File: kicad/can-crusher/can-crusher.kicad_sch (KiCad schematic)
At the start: 22 parts, among them J1 Stepper Right, J2 Control UART, J3 Ext power, J4 Stepper Left, J5 Barrel_Jack, J6 Expansion Port, Q1 IRF9540N, Q2 MMBF170, SW1 Reboot, SW2 User Interaction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

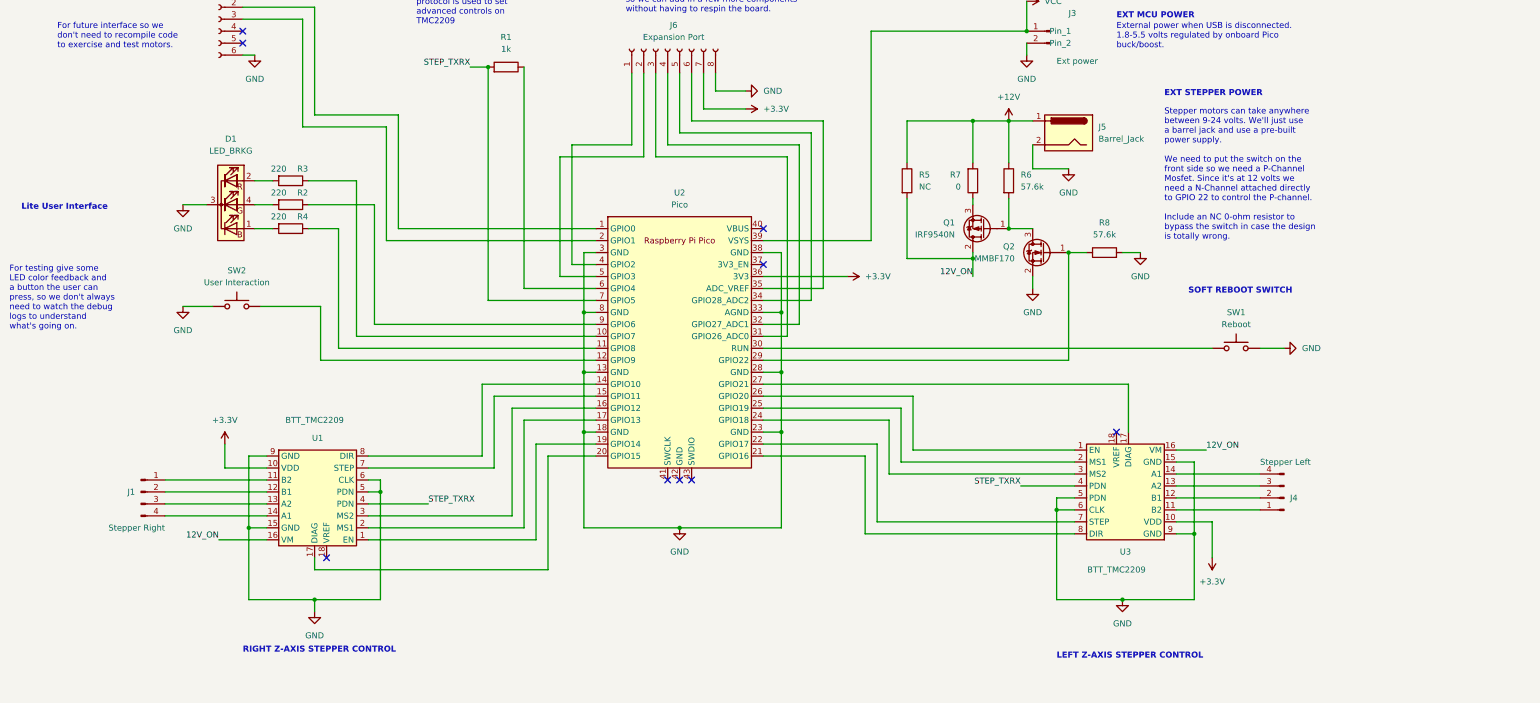
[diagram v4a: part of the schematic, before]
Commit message: Add fuse, power switch, and electrolytic caps
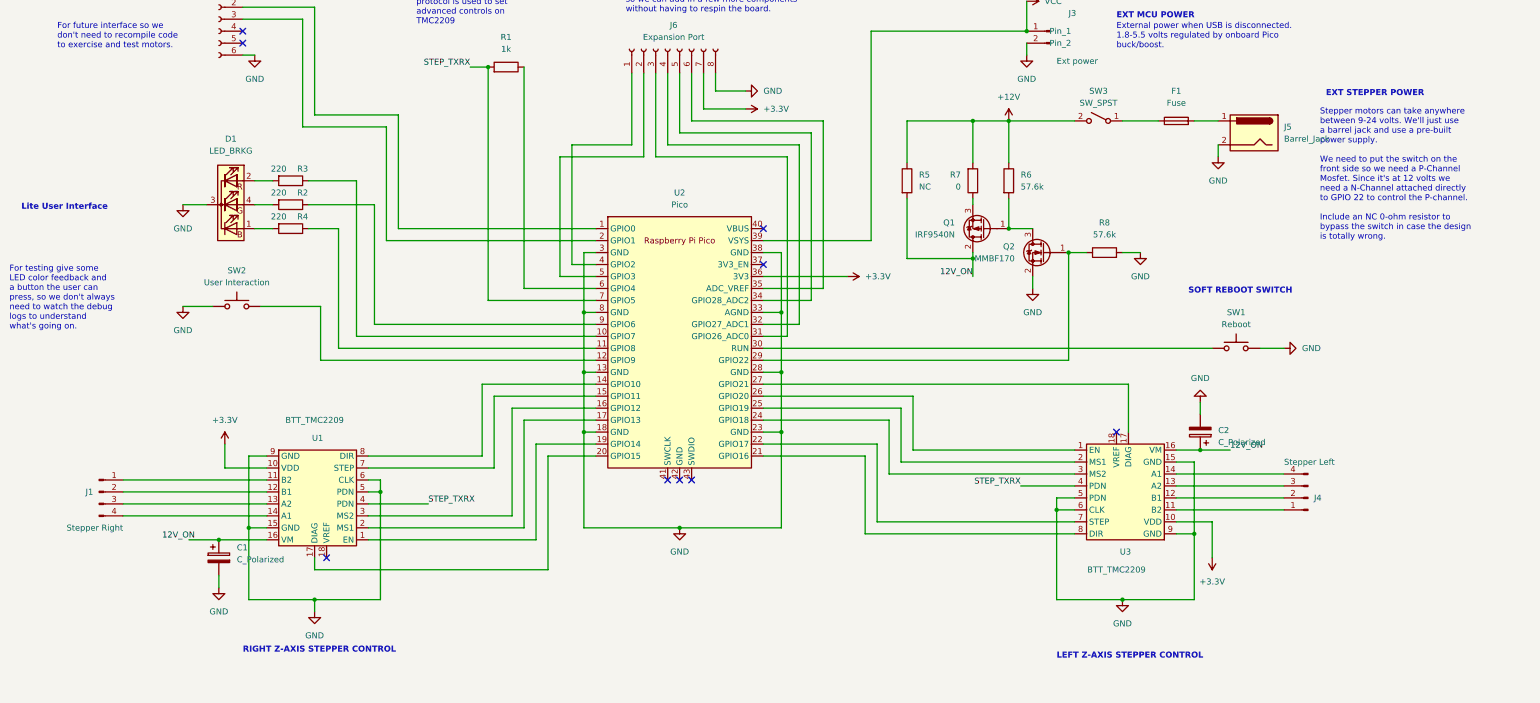
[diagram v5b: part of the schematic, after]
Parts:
- added C1, C2: C_Polarized, Capacitor_THT:CP_Radial_D6.3mm_P2.50mm, symbol Device:C_Polarized
- added F1: Fuse, Fuse:Fuse_Blade_Mini_directSolder, symbol Device:Fuse
- added SW3: SW_SPST, R1966:SW_R1966ABLKBLKGR, symbol Switch:SW_SPST
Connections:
- net +12V: now also SW3.2 (B); no longer J5.1
- net 12V_ON: now also C1.1, C2.1
- net GND: now also C1.2, C2.2
- new net: F1.1, SW3.1 (A)
- new net: F1.2, J5.1
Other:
- moved on the sheet: J1, J4, J5

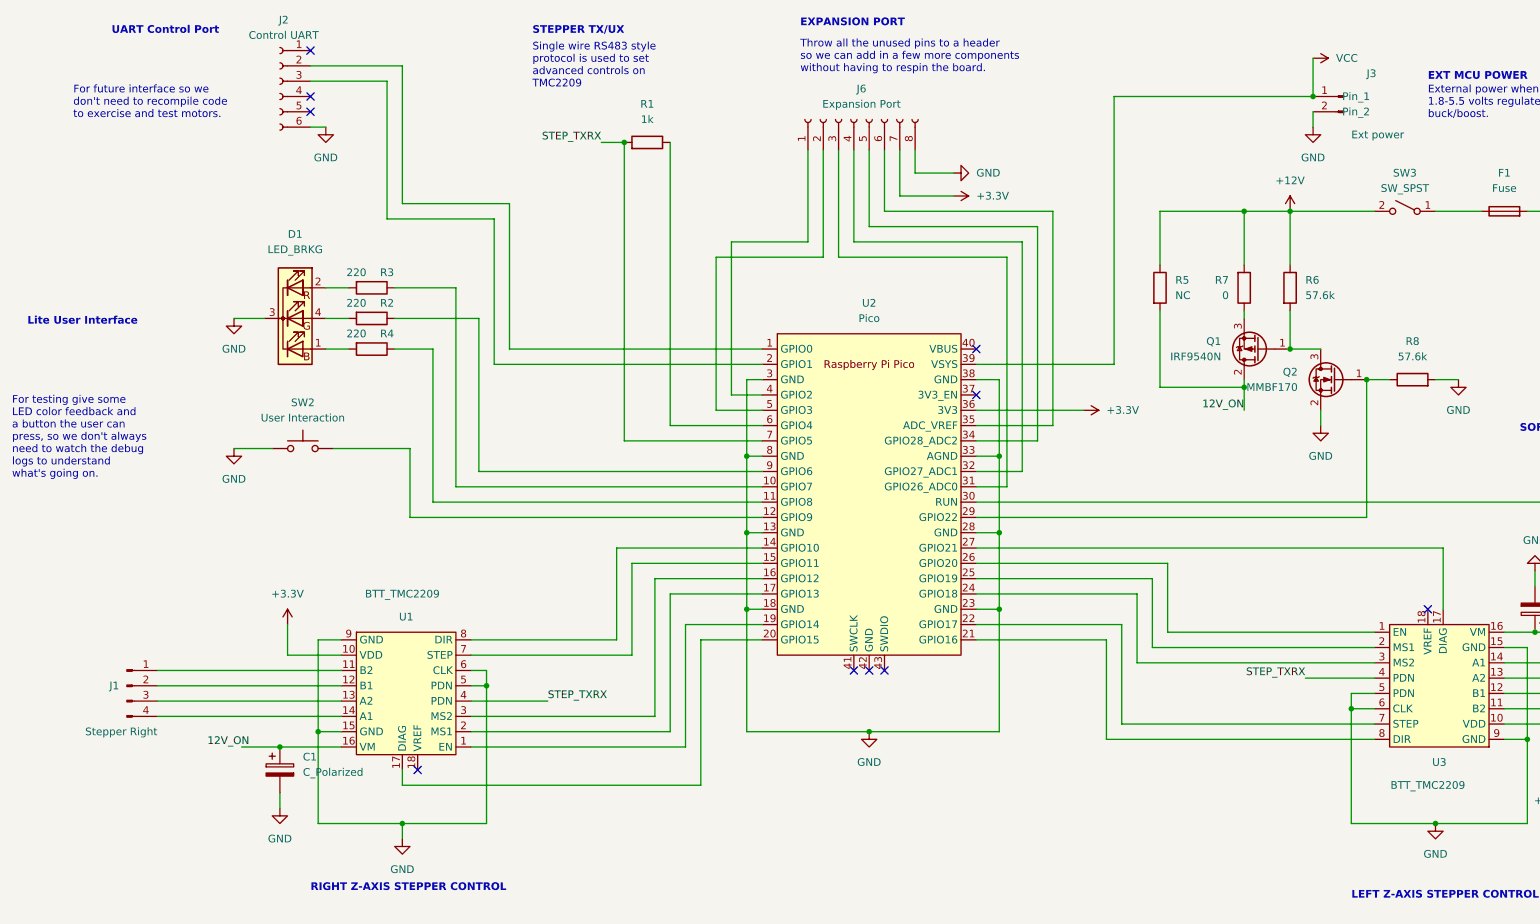
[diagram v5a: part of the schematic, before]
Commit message: Remove RGB led and button; add free pins to header; add ADC pins to the TMC2209 VREF pins for future use
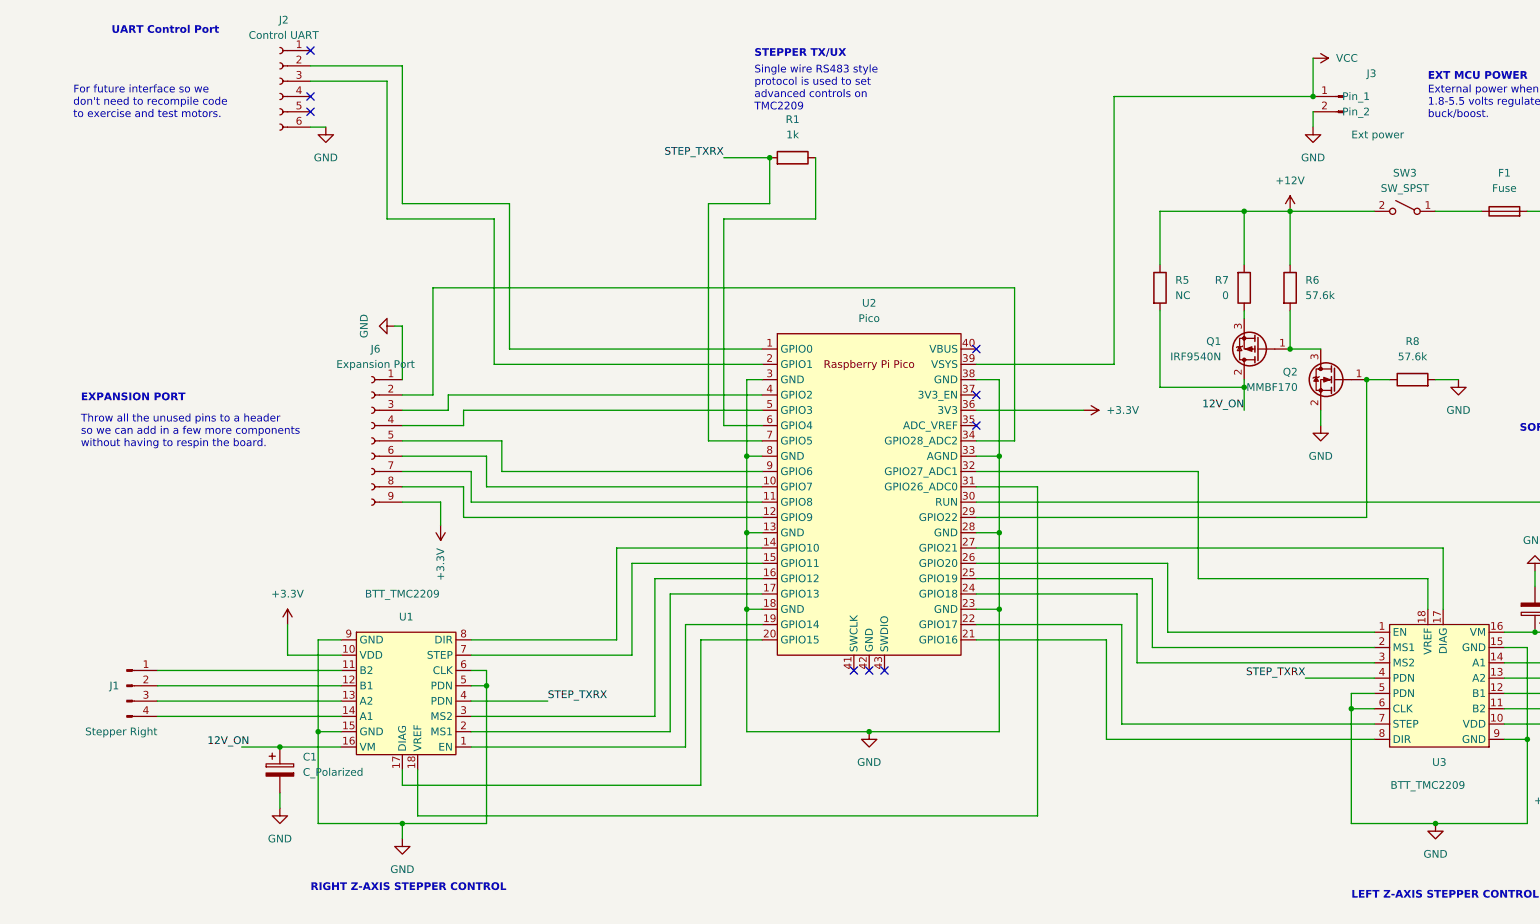
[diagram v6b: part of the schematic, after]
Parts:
- removed D1: LED_BRKG, LED_THT:LED_D5.0mm-4_RGB, symbol Device:LED_BRKG
- removed R2, R3, R4: 220, Resistor_SMD:R_0805_2012Metric, symbol Device:R
- removed SW2: User Interaction, Button_Switch_THT:SW_PUSH_6mm_H4.3mm, symbol Switch:SW_Push
- J6: footprint Connector_PinSocket_2.54mm:PinSocket_1x08_P2.54mm_Vertical -> Connector_PinSocket_2.54mm:PinSocket_1x09_P2.54mm_Vertical; symbol Connector:Conn_01x08_Female -> Connector:Conn_01x09_Female
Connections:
- net +3.3V: now also J6.9 (Pin_9); no longer J6.7 (Pin_7)
- net GND: now also J6.1 (Pin_1); no longer J6.8 (Pin_8)
- net at U2.10 (GPIO7): now also J6.6 (Pin_6)
- net at U2.9 (GPIO6): now also J6.5 (Pin_5)
- net at U1.18 (VREF): now also U2.31 (GPIO26_ADC0)
- net at U2.11 (GPIO8): now also J6.7 (Pin_7)
- net at U3.18 (VREF): now also U2.32 (GPIO27_ADC1)
- net at U2.12 (GPIO9): now also J6.8 (Pin_8)
- net at J6.3 (Pin_3): now also U2.4 (GPIO2); no longer U2.31 (GPIO26_ADC0)
- net at J6.4 (Pin_4): now also U2.5 (GPIO3); no longer U2.32 (GPIO27_ADC1)
- net at U2.34 (GPIO28_ADC2): now also J6.2 (Pin_2); no longer J6.5 (Pin_5)
- net at U2.35 (ADC_VREF): no longer J6.6 (Pin_6)
- no-connect marks 10 -> 9
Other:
- note removed: "For testing give some LED color feedback and a button the user can press, so we don't always need to watch the debug logs to understand what's going on."
- note removed: "Lite User Interface"
- moved on the sheet: R1

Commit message: Rev 2 of control PCB
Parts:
- removed F1: Fuse, Fuse:Fuse_Blade_Mini_directSolder, symbol Device:Fuse
- added C3: 100 uF, Capacitor_THT:CP_Radial_D6.3mm_P2.50mm, symbol Device:C_Polarized
- added C4: 330 uF, Capacitor_Tantalum_SMD:CP_EIA-7343-43_Kemet-X, symbol Device:C_Polarized
- added D1: 1N5819WS, Diode_SMD:D_SOD-323, symbol Diode:1N5819WS
- added L1: 330 uH, Inductor_THT:L_Radial_D12.0mm_P5.00mm_Fastron_11P, symbol Device:L
- added U4: LM2575-5.0BU, Package_TO_SOT_SMD:TO-263-5_TabPin3, symbol Regulator_Switching:LM2575-5.0BU
- added X1: 3522-2, FUSE_3522-2, symbol 3522-2:3522-2
- C1, C2: value C_Polarized -> 100 uF
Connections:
- net +12V: now also C3.1, U4.1 (VIN)
- net GND: now also C3.2, C4.2, D1.2 (A), U4.3 (GND), U4.5 (~{ON}/OFF)
- net VCC: now also C4.1, L1.2, U4.4 (FB)
- net at SW3.1 (A): now also X1.1A, X1.2A
- net at J5.1: now also X1.1B, X1.2B
- new net: D1.1 (K), L1.1, U4.2 (OUT)
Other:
- note added: "5 Volt Buck"
- moved on the sheet: J5
